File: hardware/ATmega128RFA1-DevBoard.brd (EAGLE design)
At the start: 57.1 x 53.3 mm, 50 parts, among them J1 ISP, J2 ARDUINO_UNO_R3, J3 POWER_JACKPTH_LOCK, U1 ATMEGA128RFA1, U2 LM1117, Y1 16MHz, Y2 32.768kHz

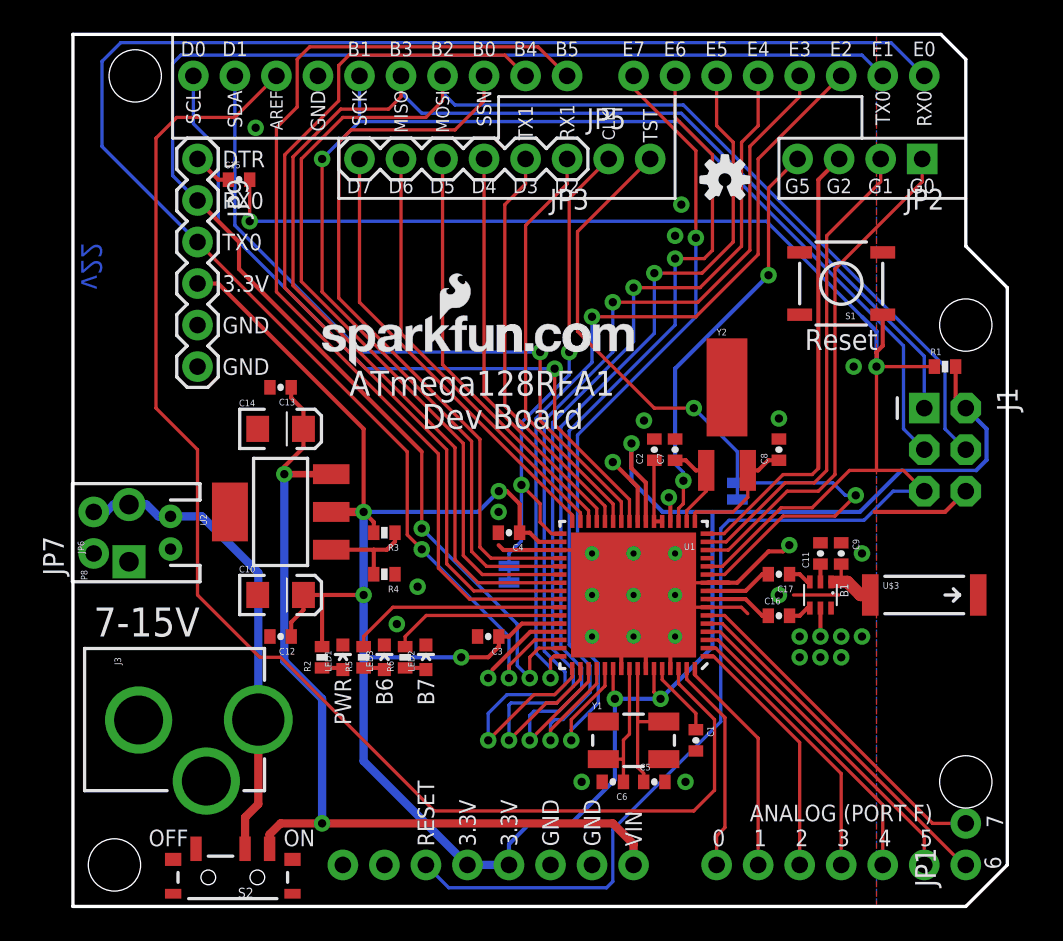
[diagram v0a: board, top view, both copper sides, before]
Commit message: Minor silkscreen fixes - v23
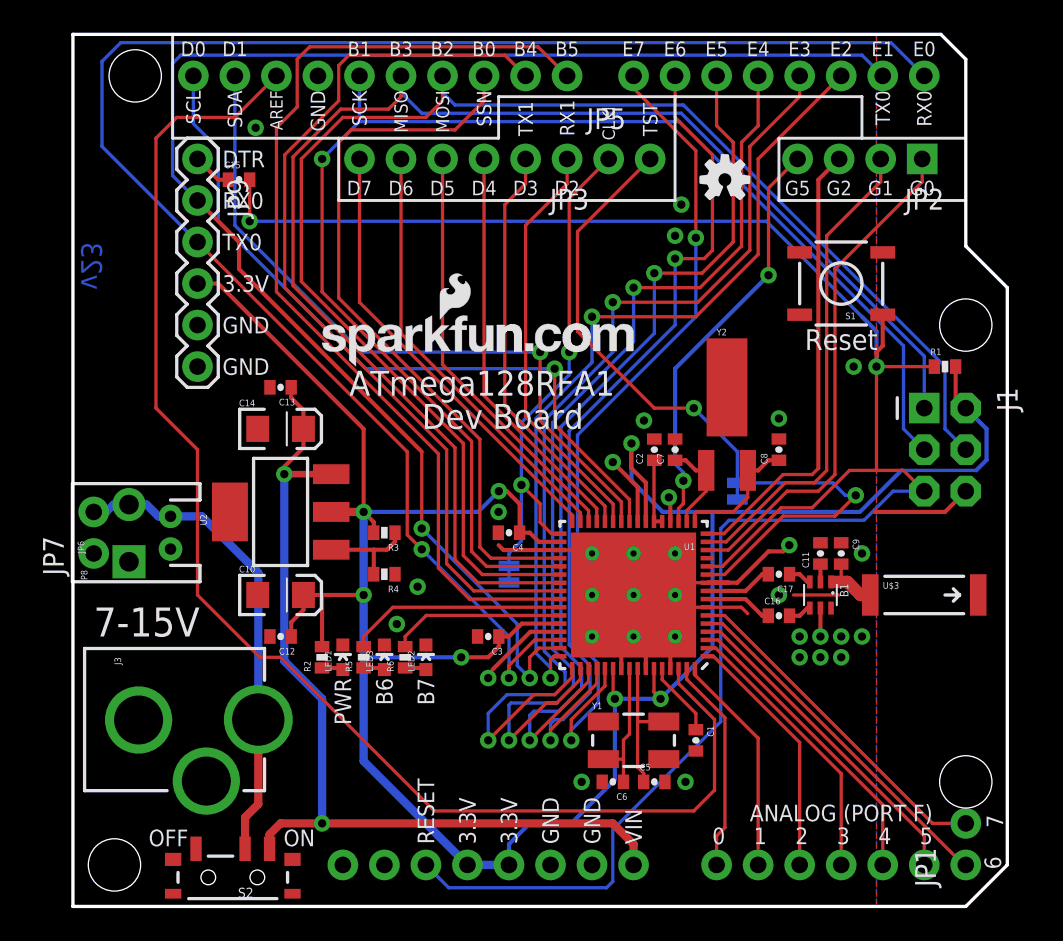
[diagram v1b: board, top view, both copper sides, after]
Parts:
- JP3: device SparkFun-Connectors:1X06 -> SparkFun-Connectors:1X06_NS
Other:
- board text added: "v23"
- board text removed: "v22"
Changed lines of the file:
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@@
 <?xml version="1.0" encoding="utf-8"?>
 <!DOCTYPE eagle SYSTEM "eagle.dtd">
-<eagle version="6.2">
+<eagle version="6.4">
 <drawing>
 <settings>
@@
 <wire x1="48.26" y1="49.53" x2="48.26" y2="46.99" width="0.1778" layer="21"/>
 <wire x1="48.26" y1="46.99" x2="54.61" y2="46.99" width="0.1778" layer="21"/>
-<text x="17.526" y="44.069" size="0.889" layer="21" font="vector" ratio="15" rot="R180" align="center">D7</text>
-<text x="20.066" y="44.069" size="0.889" layer="21" font="vector" ratio="15" align="center">D6</text>
-<text x="22.606" y="44.069" size="0.889" layer="21" font="vector" ratio="15" rot="R180" align="center">D5</text>
-<text x="25.146" y="44.069" size="0.889" layer="21" font="vector" ratio="15" align="center">D4</text>
-<text x="27.686" y="44.069" size="0.889" layer="21" font="vector" ratio="15" align="center">D3</text>
-<text x="30.226" y="44.069" size="0.889" layer="21" font="vector" ratio="15" align="center">D2</text>
-<text x="35.306" y="46.736" size="0.889" layer="21" font="vector" ratio="15" rot="R90" align="center-left">TST</text>
+<text x="17.526" y="43.942" size="0.889" layer="21" font="vector" ratio="15" rot="R180" align="center">D7</text>
+<text x="20.066" y="43.942" size="0.889" layer="21" font="vector" ratio="15" align="center">D6</text>
+<text x="22.606" y="43.942" size="0.889" layer="21" font="vector" ratio="15" rot="R180" align="center">D5</text>
+<text x="25.146" y="43.942" size="0.889" layer="21" font="vector" ratio="15" align="center">D4</text>
+<text x="27.686" y="43.942" size="0.889" layer="21" font="vector" ratio="15" align="center">D3</text>
+<text x="30.226" y="43.942" size="0.889" layer="21" font="vector" ratio="15" align="center">D2</text>
+<text x="35.306" y="47.117" size="0.889" layer="21" font="vector" ratio="15" rot="R90" align="center-left">TST</text>
 <text x="32.766" y="46.863" size="0.762" layer="21" font="vector" ratio="15" rot="R90" align="center-left">CLKI</text>
-<wire x1="16.256" y1="46.99" x2="16.256" y2="43.307" width="0.1778" layer="21"/>
-<wire x1="16.256" y1="43.307" x2="36.83" y2="43.307" width="0.1778" layer="21"/>
-<wire x1="36.83" y1="43.307" x2="36.83" y2="49.53" width="0.1778" layer="21"/>
-<text x="27.686" y="46.863" size="0.889" layer="21" font="vector" ratio="15" rot="R90" align="center-left">TX1</text>
-<text x="30.226" y="46.863" size="0.889" layer="21" font="vector" ratio="15" rot="R90" align="center-left">RX1</text>
-<text x="51.943" y="44.069" size="0.889" layer="21" font="vector" ratio="15" align="center">G0</text>
-<text x="49.403" y="44.069" size="0.889" layer="21" font="vector" ratio="15" align="center">G1</text>
-<text x="46.863" y="44.069" size="0.889" layer="21" font="vector" ratio="15" align="center">G2</text>
-<text x="44.323" y="44.069" size="0.889" layer="21" font="vector" ratio="15" align="center">G5</text>
+<wire x1="16.256" y1="46.99" x2="16.256" y2="43.18" width="0.1778" layer="21"/>
+<wire x1="16.256" y1="43.18" x2="36.83" y2="43.18" width="0.1778" layer="21"/>
+<wire x1="36.83" y1="43.18" x2="36.83" y2="49.53" width="0.1778" layer="21"/>
+<text x="27.686" y="47.117" size="0.889" layer="21" font="vector" ratio="15" rot="R90" align="center-left">TX1</text>
+<text x="30.226" y="47.117" size="0.889" layer="21" font="vector" ratio="15" rot="R90" align="center-left">RX1</text>
+<text x="51.943" y="43.942" size="0.889" layer="21" font="vector" ratio="15" align="center">G0</text>
+<text x="49.403" y="43.942" size="0.889" layer="21" font="vector" ratio="15" align="center">G1</text>
+<text x="46.863" y="43.942" size="0.889" layer="21" font="vector" ratio="15" align="center">G2</text>
+<text x="44.323" y="43.942" size="0.889" layer="21" font="vector" ratio="15" align="center">G5</text>
 <wire x1="48.26" y1="46.99" x2="43.18" y2="46.99" width="0.1778" layer="21"/>
-<wire x1="43.18" y1="46.99" x2="43.18" y2="43.307" width="0.1778" layer="21"/>
-<wire x1="43.18" y1="43.307" x2="54.61" y2="43.307" width="0.1778" layer="21"/>
+<wire x1="43.18" y1="46.99" x2="43.18" y2="43.18" width="0.1778" layer="21"/>
+<wire x1="43.18" y1="43.18" x2="54.61" y2="43.18" width="0.1778" layer="21"/>
 <wire x1="50.419" y1="31.115" x2="50.419" y2="29.845" width="0.2032" layer="21"/>
 <text x="25.019" y="32.004" size="1.524" layer="21" font="vector" ratio="15" align="center">ATmega128RFA1</text>
@@
 <text x="21.59" y="13.97" size="1.016" layer="21" font="vector" ratio="15" rot="R90" align="center-right">B7</text>
 <text x="19.05" y="13.97" size="1.016" layer="21" font="vector" ratio="15" rot="R90" align="center-right">B6</text>
-<text x="34.29" y="3.683" size="1.016" layer="21" font="vector" ratio="15" rot="R270" align="center-right">VIN</text>
-<text x="31.75" y="3.683" size="1.016" layer="21" font="vector" ratio="15" rot="R270" align="center-right">GND</text>
-<text x="29.21" y="3.683" size="1.016" layer="21" font="vector" ratio="15" rot="R270" align="center-right">GND</text>
-<text x="26.67" y="3.683" size="1.016" layer="21" font="vector" ratio="15" rot="R270" align="center-right">3.3V</text>
-<text x="24.13" y="3.683" size="1.016" layer="21" font="vector" ratio="15" rot="R270" align="center-right">3.3V</text>
-<text x="21.59" y="3.683" size="1.016" layer="21" font="vector" ratio="15" rot="R270" align="center-right">RESET</text>
+<text x="34.29" y="3.81" size="1.016" layer="21" font="vector" ratio="15" rot="R270" align="center-right">VIN</text>
+<text x="31.75" y="3.81" size="1.016" layer="21" font="vector" ratio="15" rot="R270" align="center-right">GND</text>
+<text x="29.21" y="3.81" size="1.016" layer="21" font="vector" ratio="15" rot="R270" align="center-right">GND</text>
+<text x="26.67" y="3.81" size="1.016" layer="21" font="vector" ratio="15" rot="R270" align="center-right">3.3V</text>
+<text x="24.13" y="3.81" size="1.016" layer="21" font="vector" ratio="15" rot="R270" align="center-right">3.3V</text>
+<text x="21.59" y="3.81" size="1.016" layer="21" font="vector" ratio="15" rot="R270" align="center-right">RESET</text>
 <text x="46.99" y="5.715" size="1.016" layer="21" font="vector" ratio="15" align="center">ANALOG (PORT F)</text>
-<text x="42.037" y="4.191" size="1.016" layer="21" font="vector" ratio="15" align="center">1</text>
-<text x="44.577" y="4.191" size="1.016" layer="21" font="vector" ratio="15" align="center">2</text>
-<text x="47.117" y="4.191" size="1.016" layer="21" font="vector" ratio="15" align="center">3</text>
-<text x="49.657" y="4.191" size="1.016" layer="21" font="vector" ratio="15" align="center">4</text>
-<text x="52.197" y="4.191" size="1.016" layer="21" font="vector" ratio="15" align="center">5</text>
+<text x="42.037" y="4.318" size="1.016" layer="21" font="vector" ratio="15" align="center">1</text>
+<text x="44.577" y="4.318" size="1.016" layer="21" font="vector" ratio="15" align="center">2</text>
+<text x="47.117" y="4.318" size="1.016" layer="21" font="vector" ratio="15" align="center">3</text>
+<text x="49.657" y="4.318" size="1.016" layer="21" font="vector" ratio="15" align="center">4</text>
+<text x="52.197" y="4.318" size="1.016" layer="21" font="vector" ratio="15" align="center">5</text>
 <text x="56.261" y="2.667" size="1.016" layer="21" font="vector" ratio="15" rot="R90" align="center">6</text>
 <text x="56.388" y="5.207" size="1.016" layer="21" font="vector" ratio="15" rot="R90" align="center">7</text>
-<text x="39.497" y="4.191" size="1.016" layer="21" font="vector" ratio="15" align="center">0</text>
+<text x="39.497" y="4.318" size="1.016" layer="21" font="vector" ratio="15" align="center">0</text>
 <text x="13.843" y="4.191" size="1.016" layer="21" font="vector" ratio="15" align="center">ON</text>
 <text x="5.842" y="4.191" size="1.016" layer="21" font="vector" ratio="15" align="center">OFF</text>
 <text x="1.27" y="16.51" size="1.778" layer="21" font="vector" ratio="15">7-15V</text>
-<text x="0.508" y="37.719" size="1.27" layer="16" font="vector" ratio="15" rot="MR90">v22</text>
+<text x="0.508" y="37.719" size="1.27" layer="16" font="vector" ratio="15" rot="MR90">v23</text>
 <text x="46.99" y="34.671" size="1.27" layer="21" font="vector" ratio="15" align="center">Reset</text>
 <text x="40.64" y="23.368" size="1.27" layer="22" font="vector" ratio="15" rot="MR0" align="center">TST</text>
@@
 </class>
 </classes>
-<designrules>
+<designrules name="SparkFun">
 <description language="en">&lt;b&gt;EAGLE Design Rules&lt;/b&gt;
 &lt;p&gt;
@@
 <param name="mdDrill" value="8mil"/>
 <param name="mdSmdStop" value="0mil"/>
-<param name="msWidth" value="8mil"/>
-<param name="msDrill" value="20mil"/>
+<param name="msWidth" value="7mil"/>
+<param name="msDrill" value="15mil"/>
 <param name="msMicroVia" value="9.99mm"/>
 <param name="msBlindViaRatio" value="0.5"/>
@@
 <element name="JP1" library="SparkFun-Connectors" package="1X02_NO_SILK" value="" x="54.61" y="2.54" rot="R90"/>
 <element name="JP2" library="SparkFun-Connectors" package="1X04_NO_SILK" value="" x="51.943" y="45.72" rot="R180"/>
-<element name="JP3" library="SparkFun-Connectors" package="1X06" value="" x="30.226" y="45.72" rot="R180"/>
+<element name="JP3" library="SparkFun-Connectors" package="1X06_NS" value="" x="30.226" y="45.72" rot="R180"/>
 <element name="SJ1" library="SparkFun-Passives" package="SJ_2S-TRACE" value="" x="26.67" y="20.32" rot="MR90"/>
 <element name="SJ2" library="SparkFun-Passives" package="SJ_2S-TRACE" value="" x="40.64" y="25.4" rot="MR90"/>

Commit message: More minor silkscreen fixes
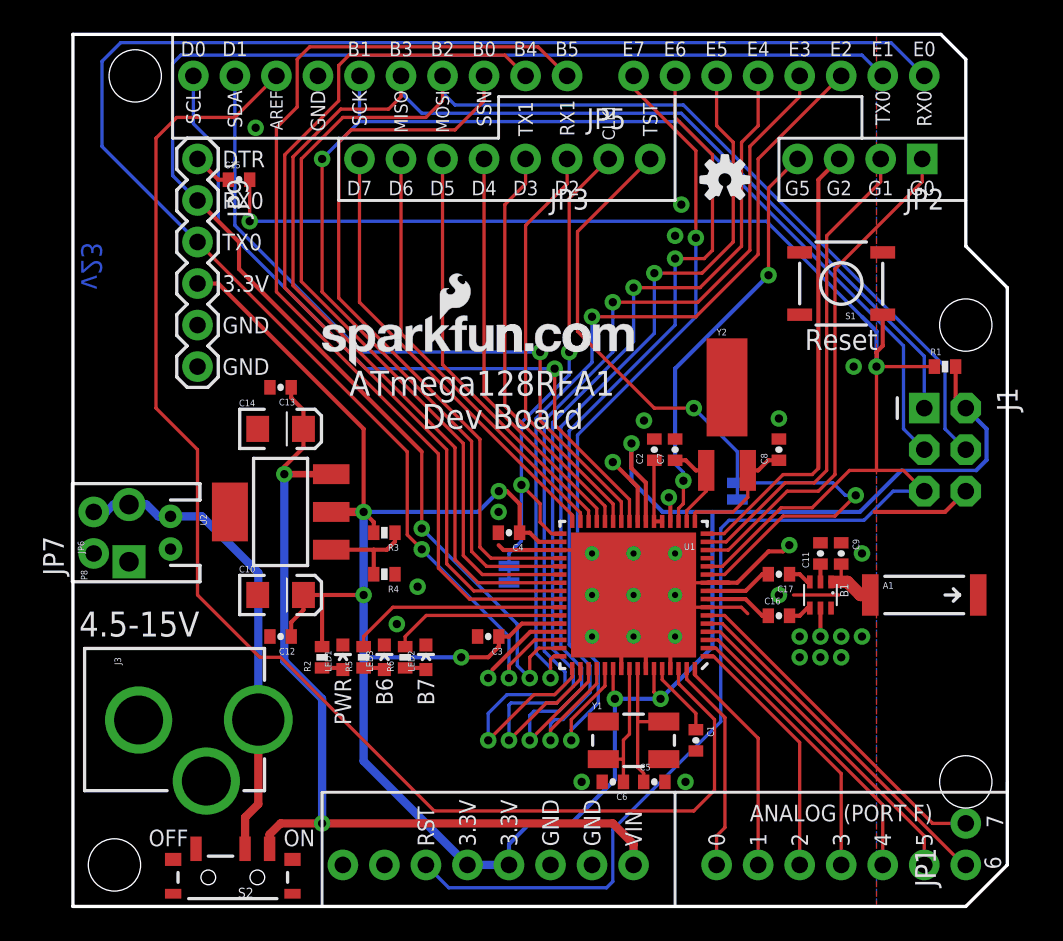
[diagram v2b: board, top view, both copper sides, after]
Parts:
- renumbered U$3 to A1
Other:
- board text added: "4.5-15V"
- board text added: "RST"
- board text removed: "7-15V"
- board text removed: "RESET"
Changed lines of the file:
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@@
 <text x="21.59" y="13.97" size="1.016" layer="21" font="vector" ratio="15" rot="R90" align="center-right">B7</text>
 <text x="19.05" y="13.97" size="1.016" layer="21" font="vector" ratio="15" rot="R90" align="center-right">B6</text>
-<text x="34.29" y="3.81" size="1.016" layer="21" font="vector" ratio="15" rot="R270" align="center-right">VIN</text>
-<text x="31.75" y="3.81" size="1.016" layer="21" font="vector" ratio="15" rot="R270" align="center-right">GND</text>
-<text x="29.21" y="3.81" size="1.016" layer="21" font="vector" ratio="15" rot="R270" align="center-right">GND</text>
-<text x="26.67" y="3.81" size="1.016" layer="21" font="vector" ratio="15" rot="R270" align="center-right">3.3V</text>
-<text x="24.13" y="3.81" size="1.016" layer="21" font="vector" ratio="15" rot="R270" align="center-right">3.3V</text>
-<text x="21.59" y="3.81" size="1.016" layer="21" font="vector" ratio="15" rot="R270" align="center-right">RESET</text>
+<text x="34.29" y="3.683" size="1.016" layer="21" font="vector" ratio="15" rot="R270" align="center-right">VIN</text>
+<text x="31.75" y="3.683" size="1.016" layer="21" font="vector" ratio="15" rot="R270" align="center-right">GND</text>
+<text x="29.21" y="3.683" size="1.016" layer="21" font="vector" ratio="15" rot="R270" align="center-right">GND</text>
+<text x="26.67" y="3.683" size="1.016" layer="21" font="vector" ratio="15" rot="R270" align="center-right">3.3V</text>
+<text x="24.13" y="3.683" size="1.016" layer="21" font="vector" ratio="15" rot="R270" align="center-right">3.3V</text>
+<text x="21.59" y="3.683" size="1.016" layer="21" font="vector" ratio="15" rot="R270" align="center-right">RST</text>
 <text x="46.99" y="5.715" size="1.016" layer="21" font="vector" ratio="15" align="center">ANALOG (PORT F)</text>
-<text x="42.037" y="4.318" size="1.016" layer="21" font="vector" ratio="15" align="center">1</text>
-<text x="44.577" y="4.318" size="1.016" layer="21" font="vector" ratio="15" align="center">2</text>
-<text x="47.117" y="4.318" size="1.016" layer="21" font="vector" ratio="15" align="center">3</text>
-<text x="49.657" y="4.318" size="1.016" layer="21" font="vector" ratio="15" align="center">4</text>
-<text x="52.197" y="4.318" size="1.016" layer="21" font="vector" ratio="15" align="center">5</text>
+<text x="41.91" y="3.683" size="1.016" layer="21" font="vector" ratio="15" rot="R90" align="center-left">1</text>
+<text x="44.45" y="3.683" size="1.016" layer="21" font="vector" ratio="15" rot="R90" align="center-left">2</text>
+<text x="46.99" y="3.683" size="1.016" layer="21" font="vector" ratio="15" rot="R90" align="center-left">3</text>
+<text x="49.53" y="3.683" size="1.016" layer="21" font="vector" ratio="15" rot="R90" align="center-left">4</text>
+<text x="52.07" y="3.683" size="1.016" layer="21" font="vector" ratio="15" rot="R90" align="center-left">5</text>
 <text x="56.261" y="2.667" size="1.016" layer="21" font="vector" ratio="15" rot="R90" align="center">6</text>
 <text x="56.388" y="5.207" size="1.016" layer="21" font="vector" ratio="15" rot="R90" align="center">7</text>
-<text x="39.497" y="4.318" size="1.016" layer="21" font="vector" ratio="15" align="center">0</text>
+<text x="39.37" y="3.683" size="1.016" layer="21" font="vector" ratio="15" rot="R90" align="center-left">0</text>
 <text x="13.843" y="4.191" size="1.016" layer="21" font="vector" ratio="15" align="center">ON</text>
 <text x="5.842" y="4.191" size="1.016" layer="21" font="vector" ratio="15" align="center">OFF</text>
-<text x="1.27" y="16.51" size="1.778" layer="21" font="vector" ratio="15">7-15V</text>
+<text x="0.381" y="16.51" size="1.524" layer="21" font="vector" ratio="15">4.5-15V</text>
 <text x="0.508" y="37.719" size="1.27" layer="16" font="vector" ratio="15" rot="MR90">v23</text>
 <text x="46.99" y="34.671" size="1.27" layer="21" font="vector" ratio="15" align="center">Reset</text>
@@
 <wire x1="57.15" y1="2.54" x2="57.15" y2="37.846" width="0.2032" layer="20"/>
 <wire x1="57.15" y1="37.846" x2="54.61" y2="40.386" width="0.2032" layer="20"/>
+<wire x1="15.24" y1="0" x2="15.24" y2="6.985" width="0.1778" layer="21"/>
+<wire x1="15.24" y1="6.985" x2="36.83" y2="6.985" width="0.1778" layer="21"/>
+<wire x1="36.83" y1="6.985" x2="57.15" y2="6.985" width="0.1778" layer="21"/>
+<wire x1="57.15" y1="6.985" x2="57.15" y2="7.62" width="0.1778" layer="21"/>
+<wire x1="36.83" y1="0" x2="36.83" y2="6.985" width="0.1778" layer="21"/>
 </plain>
 <attributes>
@@
 <element name="R6" library="SparkFun" package="0402-RES" value="330" x="20.32" y="15.24" rot="R90"/>
 <element name="JP4" library="SparkFun-Aesthetics" package="SFE-NEW-WEBLOGO" value="LOGO-SFENEW" x="33.02" y="26.67" rot="MR0"/>
-<element name="U$3" library="SparkFun-RF" package="ANTENNA-CHIP5" value="ANTENNA2SMD5" x="52.07" y="19.05" smashed="yes">
+<element name="A1" library="SparkFun-RF" package="ANTENNA-CHIP5" value="ANTENNA2SMD5" x="52.07" y="19.05" smashed="yes">
 <attribute name="NAME" x="49.53" y="19.431" size="0.4064" layer="25"/>
 <attribute name="VALUE" x="49.53" y="18.288" size="0.4064" layer="27"/>
@@
 <wire x1="46.37" y1="19.85" x2="46.571" y2="19.85" width="0.254" layer="1"/>
 <wire x1="46.571" y1="19.85" x2="46.99" y2="19.85" width="0.762" layer="1"/>
-<contactref element="U$3" pad="FEED"/>
+<contactref element="A1" pad="FEED"/>
 <wire x1="46.99" y1="19.85" x2="47.371" y2="19.85" width="0.762" layer="1"/>
 <wire x1="48.171" y1="19.05" x2="47.371" y2="19.85" width="0.762" layer="1"/>
